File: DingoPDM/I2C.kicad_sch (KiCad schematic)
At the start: 64 parts, among them U10 MCP9808, U12 ADS1015, U13 PCA9539, U14 PCA9635, U15 MB85RC256V, U16 ADS1015, U17 PCAL9554B, U20 PCA9539

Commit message: Swapped to AMPSEAL 14 pins
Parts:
- renumbered C29 to C10, C71 to C11, C67 to C12, C69 to C13, C36 to C14, C68 to C15, C30 to C16, C31 to C17, C32 to C18, C70 to C19, C40 to C20, C37 to C21, C39 to C22, D44 to D11, D20 to D12, D21 to D13, D22 to D14, D23 to D15, D24 to D16, D25 to D17, D26 to D18, D27 to D19, D28 to D20, D29 to D21, D30 to D22, D31 to D23, D32 to D24, D33 to D25, D34 to D26, D35 to D27, R59 to R17, R60 to R18, R105 to R19, R106 to R20, R93 to R21, R64 to R22, R72 to R23, R73 to R24, R74 to R25, R75 to R26, R65 to R27, R77 to R28, R78 to R29, R79 to R30, R80 to R31, R81 to R32, R82 to R33, R83 to R34, R84 to R35, R85 to R36, R86 to R37, R87 to R38, TP7 to TP1, TP8 to TP2, TP9 to TP3, TP10 to TP4, U12 to U1, U16 to U2, U13 to U3, U20 to U4, U15 to U5, U10 to U6, U17 to U7, U14 to U8

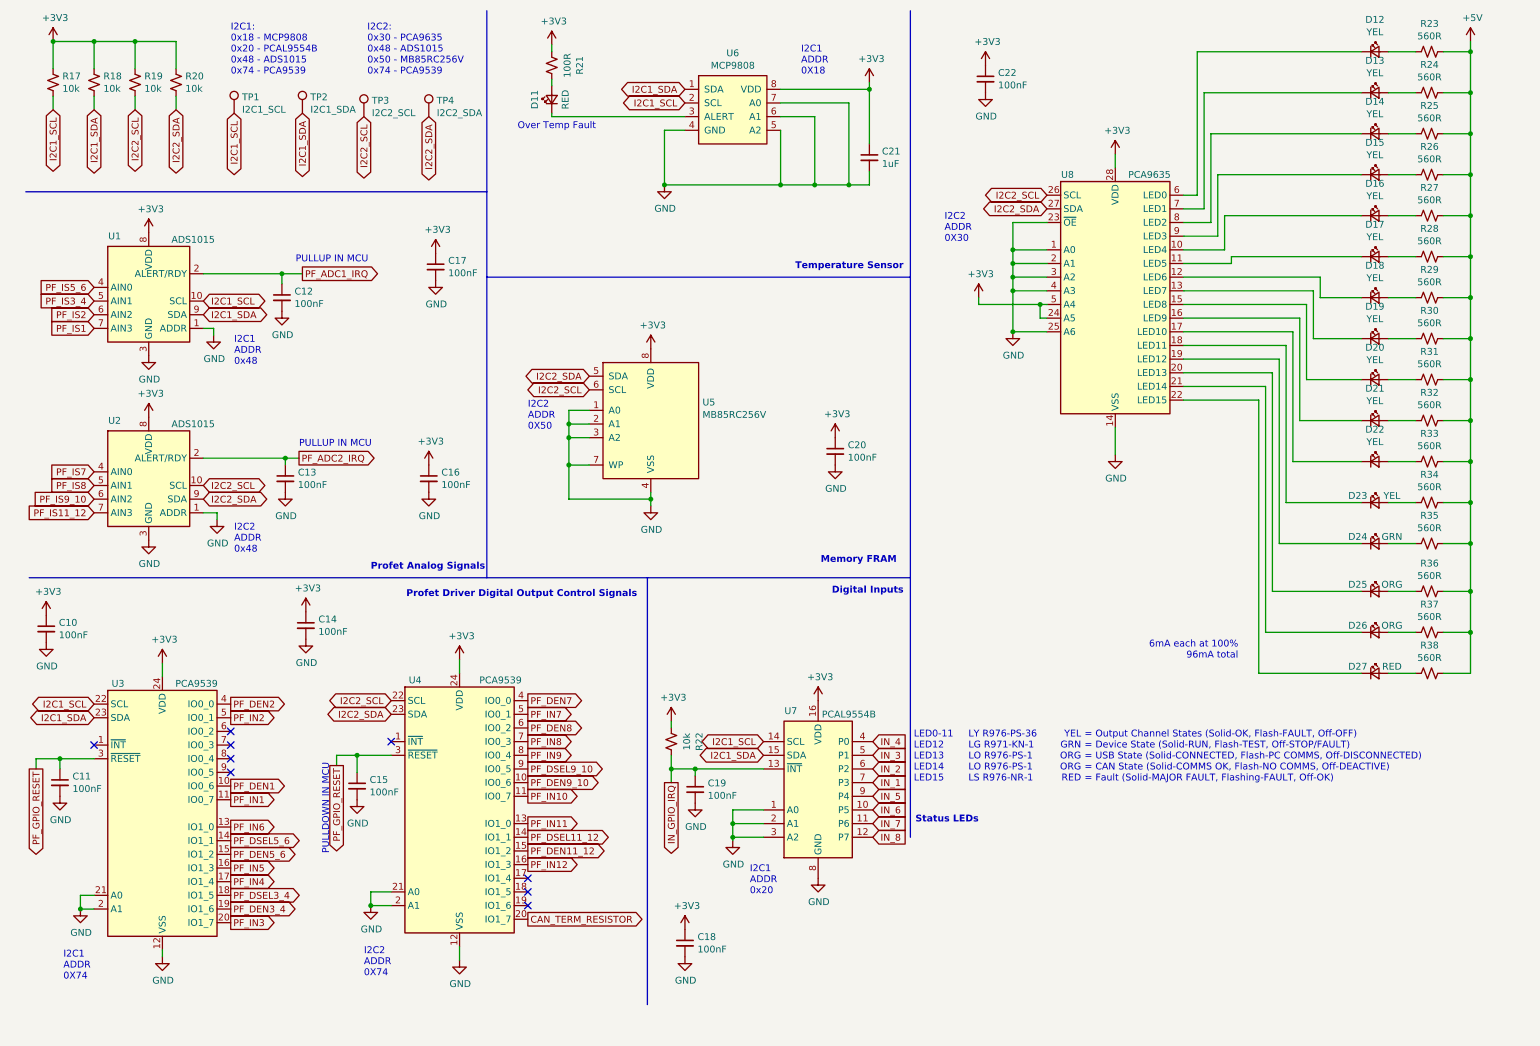
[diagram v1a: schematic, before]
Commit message: Removed unused IRQs, added pd res on PF GPIO reset
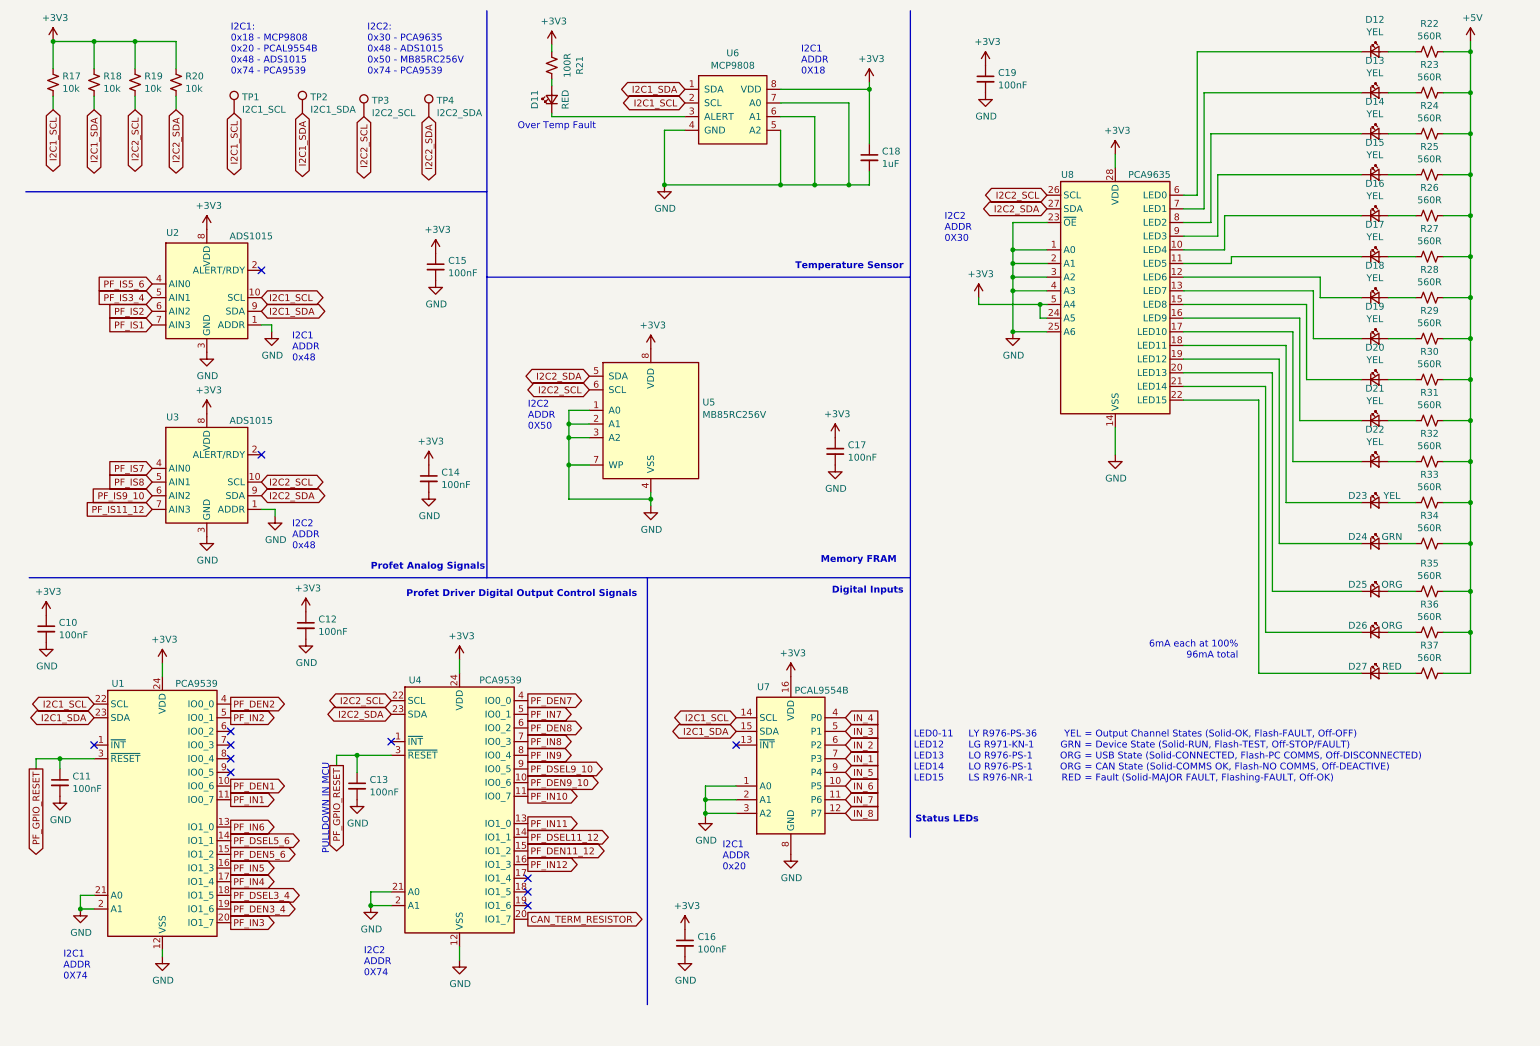
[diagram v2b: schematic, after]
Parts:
- removed C12, C13, C19: 100nF, Capacitor_SMD:C_0805_2012Metric, symbol Device:C_Small
- removed R22: 10k, Resistor_SMD:R_0805_2012Metric, symbol Device:R_Small_US
- renumbered C14 to C12, C15 to C13, C16 to C14, C17 to C15, C18 to C16, C20 to C17, C21 to C18, C22 to C19, R23 to R22, R24 to R23, R25 to R24, R26 to R25, R27 to R26, R28 to R27, R29 to R28, R30 to R29, R31 to R30, R32 to R31, R33 to R32, R34 to R33, R35 to R34, R36 to R35, R37 to R36, R38 to R37, U3 to U1, U1 to U2, U2 to U3
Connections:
- net IN_GPIO_IRQ: no longer names the net of U7.13 (~{INT})
- net PF_ADC1_IRQ: no longer names the net of U2.2 (ALERT/RDY)
- net PF_ADC2_IRQ: no longer names the net of U3.2 (ALERT/RDY)
- no-connect marks 9 -> 12
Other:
- note removed: "PULLUP IN MCU"
- moved on the sheet: U2, U3, U7

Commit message: Added export, fixed some PNs
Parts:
- U7: Digi-Key_PN (none) -> 568-9926-1-ND
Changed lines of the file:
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@@
+      (effects (font (size 1.27 1.27)) hide)
+    )
+    (property "Digi-Key_PN" "568-9926-1-ND" (id 4) (at 154.305 151.765 0)
       (effects (font (size 1.27 1.27)) hide)
     )

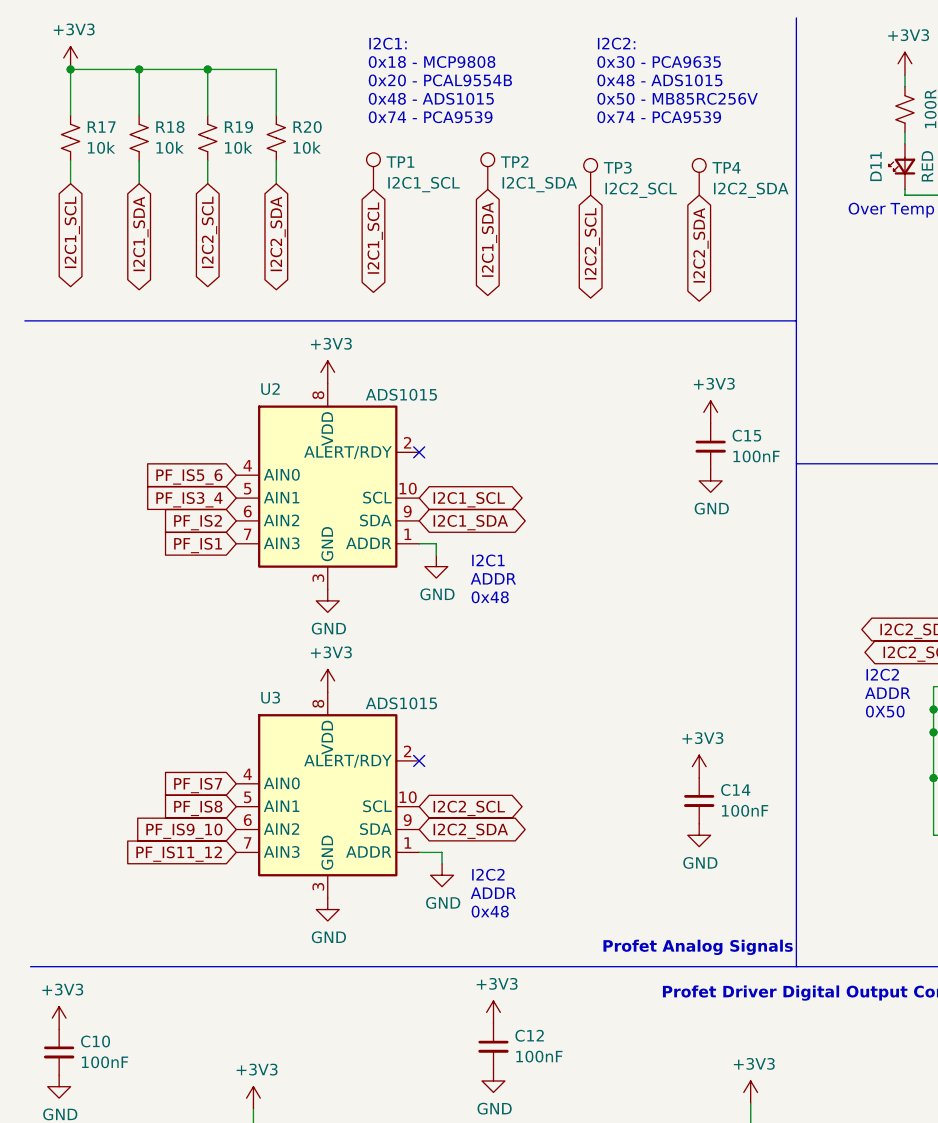
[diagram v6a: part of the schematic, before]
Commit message: V5 As Built
-Changed ADS1015 to MAX11613EUA+T due to supply issues
-Changed PCB to match JLCPCB 2oz rules
-Changed ON_SW input to 12V switched
-Switched to TagConnect TC2030
-Changed pin positions of GND, IN1, IN2
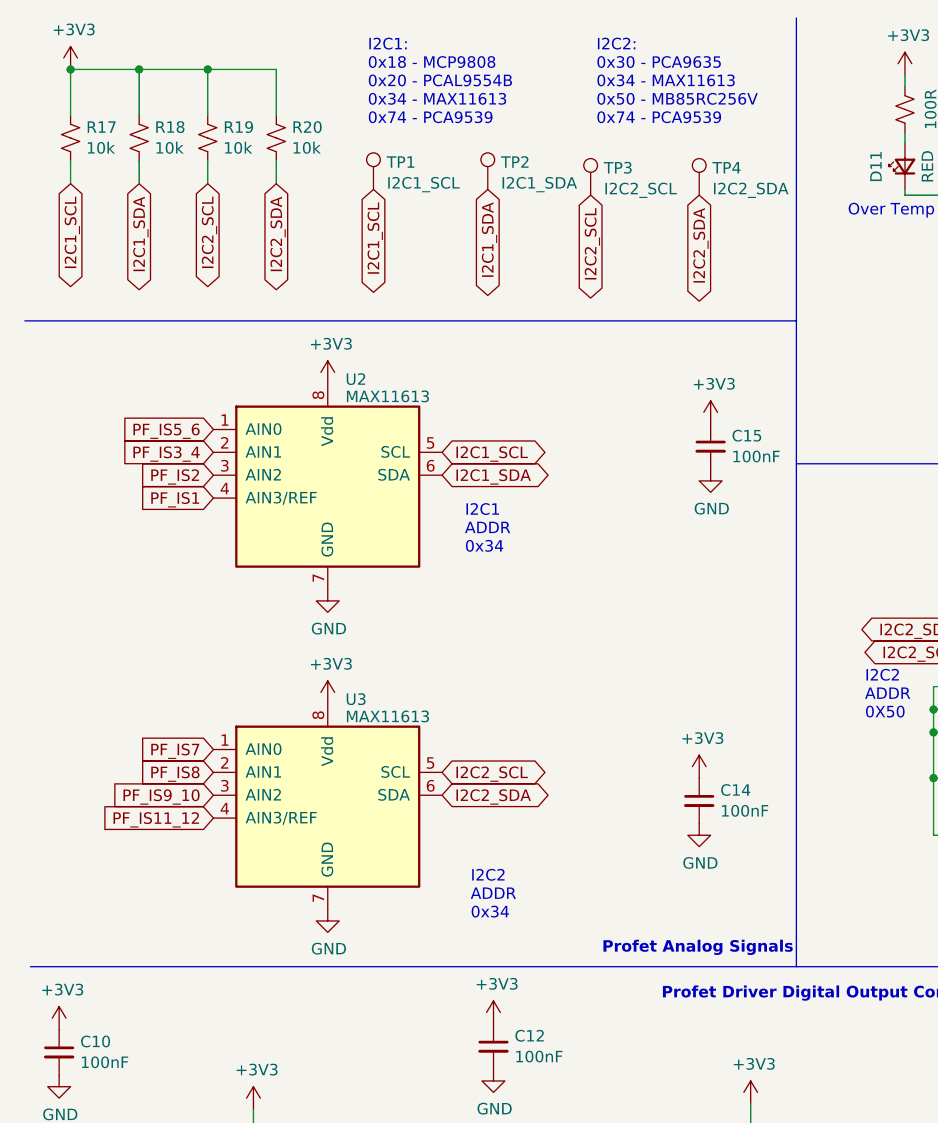
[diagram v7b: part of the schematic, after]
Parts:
- removed U2, U3: ADS1015, Package_SO:VSSOP-10_3x3mm_P0.5mm, symbol Analog_ADC:ADS1015IDGS
- added U2, U3: MAX11613, Package_SO:MSOP-8_3x3mm_P0.65mm, symbol Analog_ADC:MAX11613
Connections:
- net +3V3: now also U2.8 (Vdd), U3.8 (Vdd)
- net GND: now also U2.7 (GND), U3.7 (GND)
- net I2C1_SCL: now also U2.5 (SCL)
- net I2C1_SDA: now also U2.6 (SDA)
- net I2C2_SCL: now also U3.5 (SCL)
- net I2C2_SDA: now also U3.6 (SDA)
- net PF_IS1: now also U2.4 (AIN3/REF)
- net PF_IS11_12: now also U3.4 (AIN3/REF)
- net PF_IS2: now also U2.3 (AIN2)
- net PF_IS3_4: now also U2.2 (AIN1)
- net PF_IS5_6: now also U2.1 (AIN0)
- net PF_IS7: now also U3.1 (AIN0)
- net PF_IS8: now also U3.2 (AIN1)
- net PF_IS9_10: now also U3.3 (AIN2)
- no-connect marks 12 -> 10
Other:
- note added: "I2C1 ADDR 0x34"
- note added: "I2C1: 0x18 - MCP9808 0x20 - PCAL9554B 0x34 - MAX11613 0x74 - PCA9539"
- note added: "I2C2 ADDR 0x34"
- note added: "I2C2: 0x30 - PCA9635 0x34 - MAX11613 0x50 - MB85RC256V 0x74 - PCA9539"
- note removed: "I2C1 ADDR 0x48"
- note removed: "I2C1: 0x18 - MCP9808 0x20 - PCAL9554B 0x48 - ADS1015 0x74 - PCA9539"
- note removed: "I2C2 ADDR 0x48"
- note removed: "I2C2: 0x30 - PCA9635 0x48 - ADS1015 0x50 - MB85RC256V 0x74 - PCA9539"
- title: (none) -> Dingo_PDM

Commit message: Changed schematic sheet size to letter
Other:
- note added: "= Output Channel States (Solid-OK, Flash-FAULT, Off-OFF) = Device State (Solid-RUN, Flash-TEST, Off-STOP/FAULT) = USB State (Solid-CONNECTED, Flash-COMMS, Off-DISCONNECTED) = CAN State (Solid-COMMS OK, Flash-NO COMMS, Off-DEACTIVE) = Fault (Solid-MAJOR FAULT, Flashing-FAULT, Off-OK)"
- note removed: "= Output Channel States (Solid-OK, Flash-FAULT, Off-OFF) = Device State (Solid-RUN, Flash-TEST, Off-STOP/FAULT) = USB State (Solid-CONNECTED, Flash-PC COMMS, Off-DISCONNECTED) = CAN State (Solid-COMMS OK, Flash-NO COMMS, Off-DEACTIVE) = Fault (Solid-MAJOR FAULT, Flashing-FAULT, Off-OK)"
- note removed: "LY R976-PS-36 LG R971-KN-1 LO R976-PS-1 LO R976-PS-1 LS R976-NR-1"
- moved on the sheet: C19, D12, D13, D14, D15, D16, D17, D18, D19, D20, D21, D22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
